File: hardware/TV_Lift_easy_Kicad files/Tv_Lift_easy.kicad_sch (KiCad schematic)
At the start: 103 parts, among them J1 C54620381, J10 1844210, J11 1844223, J12 C5360899, J2 1836189, J3 1844223, J4 1844210, J5 1844223, J6 1844223, J7 1844236, J8 C5360899, J9 1844210, Q2 C105432, SW1 TS-1187A-BAB, SW2 TS-1187A-BAB, SW3 TS-1187A-BAB, SW4 TS-1187A-BAB, U1 MAX3232, U10 VNH5019ATR-E, U2 C145345, U3 SN65HVD230, U4 ESP32-WROOM-32E-N16, U5 LM2596S-5, U6 AMS1117-3.3, U7 PC817, U8 PC817, U9 b0505s-1we

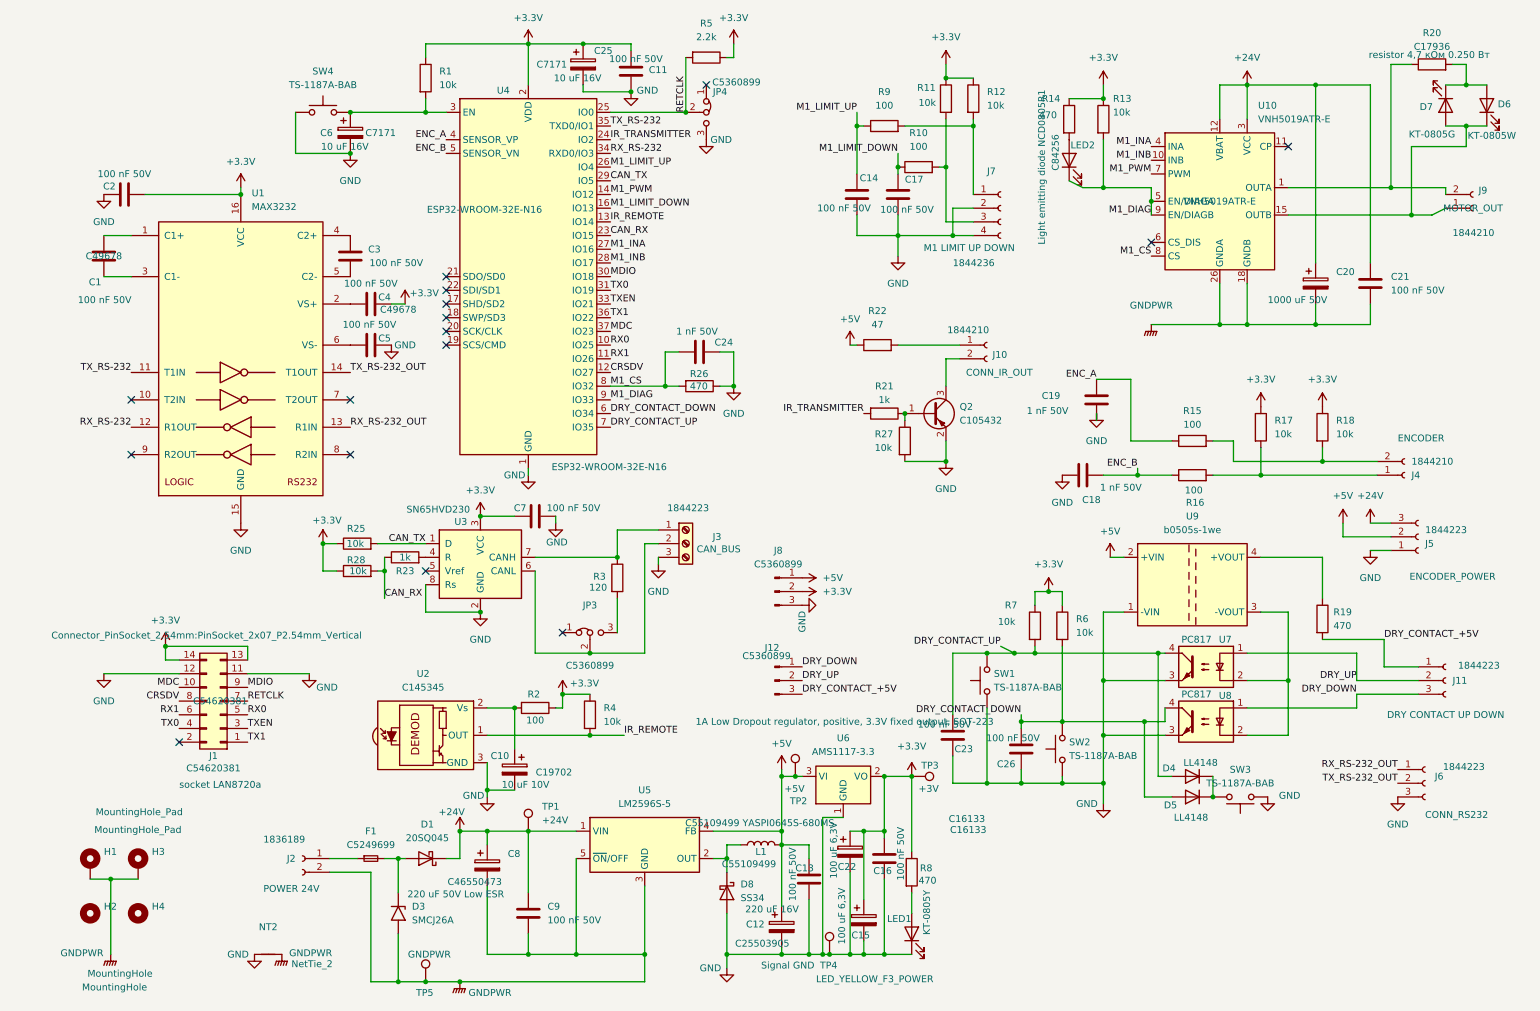
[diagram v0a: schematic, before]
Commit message: add  newe fuse easy board version
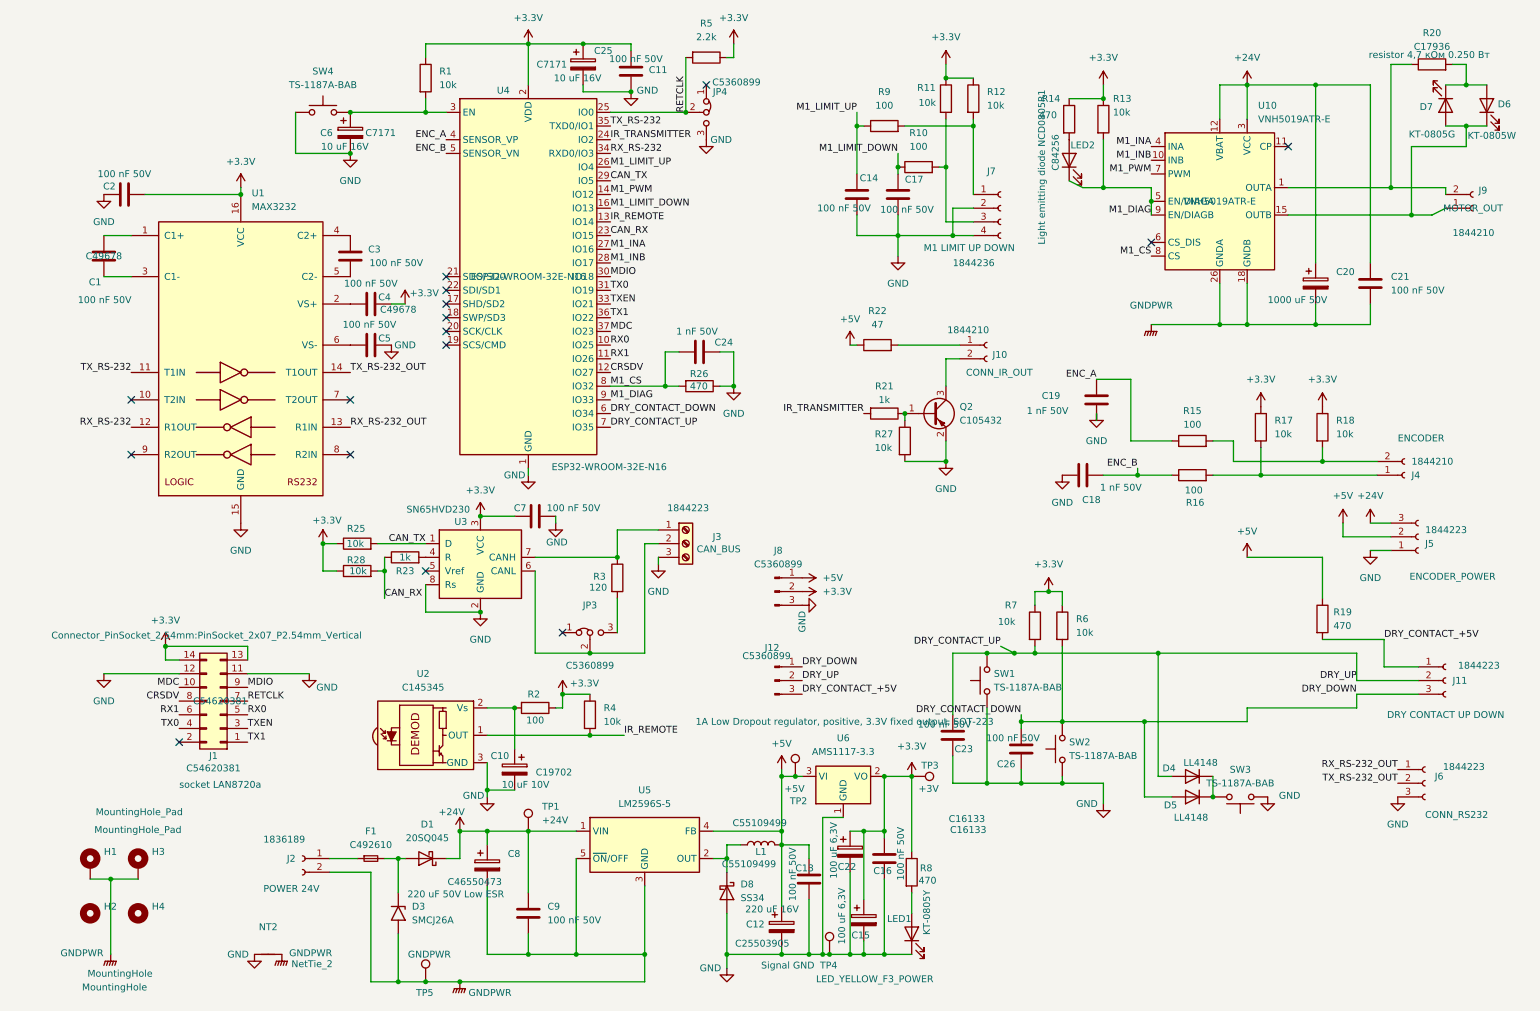
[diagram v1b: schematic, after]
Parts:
- removed U7, U8: PC817, Package_DIP:DIP-4_W7.62mm, symbol Isolator:PC817
- removed U9: b0505s-1we, Converter_DCDC:Converter_DCDC_RECOM_R-78S-0.1_THT, symbol Regulator_Switching:CRE1S0505SC
- F1: value C5249699 -> C492610; footprint Fuse:Fuseholder_Blade_Mini_Keystone_3568 -> Fuse:Fuseholder_XF-506P_mini_blade_C492610
- JP3, JP4: now in the parts list
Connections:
- net DRY_DOWN is gone; now on net DRY_CONTACT_DOWN: J11.3 (Pin_3), J12.1 (Pin_1)
- net DRY_UP is gone; now on net DRY_CONTACT_UP: J11.2 (Pin_2), J12.2 (Pin_2)
- net +5V: now also R19.1
